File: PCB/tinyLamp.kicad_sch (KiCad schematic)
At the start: 21 parts, among them J11 USB_B_Mini, J12 Conn_02x03_Odd_Even, SW11 SW_Push, SW12 SW_Push, SW13 SW_Push, U11 TP4056, U12 ATtiny24A-SS, X11 BATT+, X12 BATT-

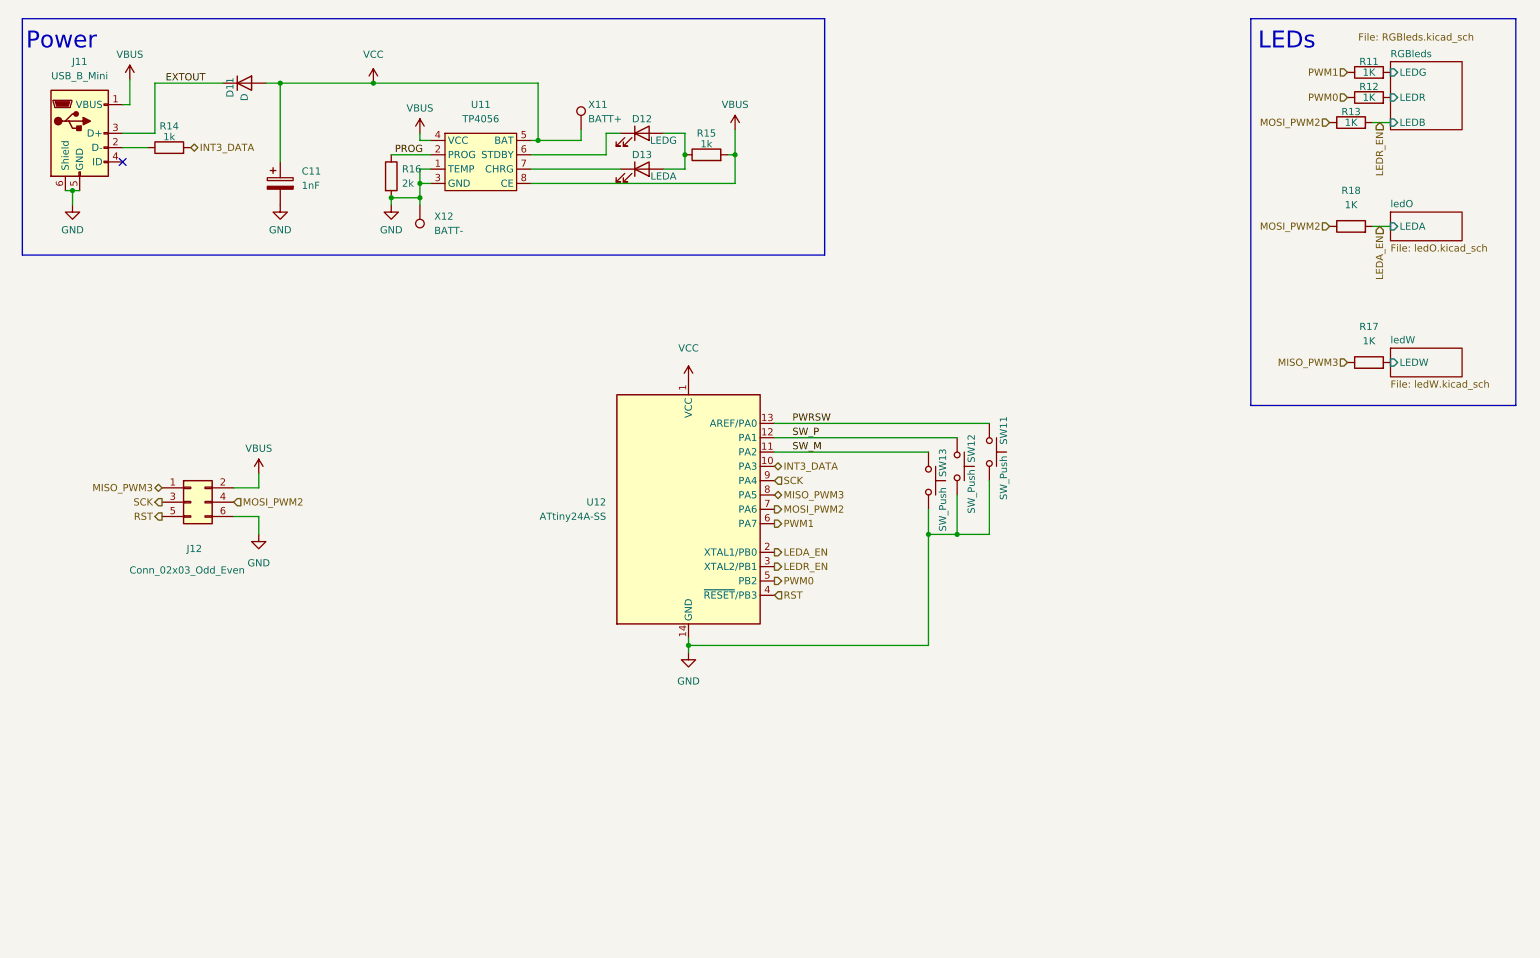
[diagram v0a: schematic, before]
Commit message: Updated Schematic to use Wemos D1 and external Power
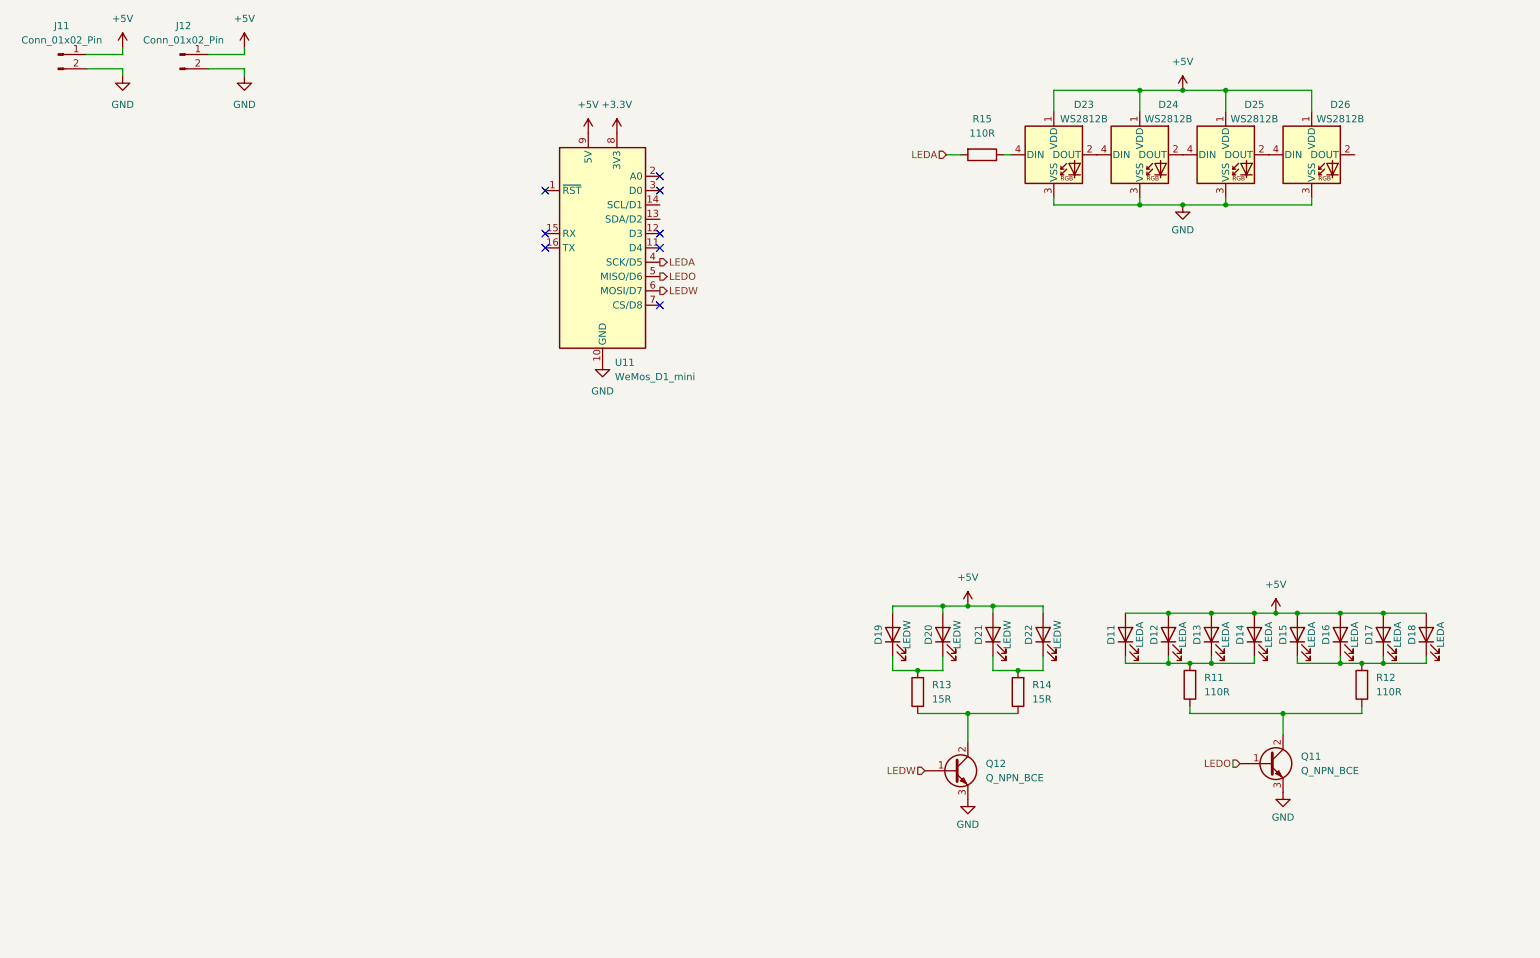
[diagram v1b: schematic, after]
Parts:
- removed C11: 1nF, Capacitor_SMD:C_1206_3216Metric_Pad1.33x1.80mm_HandSolder, symbol Device:C_Polarized
- removed D11: D, Diode_SMD:D_SOD-123, symbol Device:D
- removed J11: USB_B_Mini, Connector_USB:USB_Mini-B_Lumberg_2486_01_Horizontal, symbol Connector:USB_B_Mini
- removed J12: Conn_02x03_Odd_Even, Connector_PinHeader_2.54mm:PinHeader_2x03_P2.54mm_Vertical, symbol Connector_Generic:Conn_02x03_Odd_Even
- removed R16: 2k, Resistor_SMD:R_1206_3216Metric_Pad1.30x1.75mm_HandSolder, symbol Device:R
- removed R17, R18: 1K, Resistor_SMD:R_1206_3216Metric_Pad1.30x1.75mm_HandSolder, symbol Device:R
- removed SW11, SW12, SW13: SW_Push, Button_Switch_SMD:SW_SPST_CK_RS282G05A3, symbol Switch:SW_Push
- removed U11: TP4056, Package_SO:HSOP-8-1EP_3.9x4.9mm_P1.27mm_EP2.3x2.3mm, symbol BatteryProtection:TP4056
- removed U12: ATtiny24A-SS, Package_SO:SOIC-14_3.9x8.7mm_P1.27mm, symbol MCU_Microchip_ATtiny:ATtiny24A-SS
- removed X11: BATT+, TestPoint:TestPoint_Keystone_5015_Micro-Minature, symbol Connector:TestPoint
- removed X12: BATT-, TestPoint:TestPoint_Keystone_5015_Micro-Minature, symbol Connector:TestPoint
- added D11, D14, D15, D16, D17, D18: LEDA, LED_SMD:LED_0805_2012Metric_Pad1.15x1.40mm_HandSolder, symbol Device:LED
- added D19, D20, D21, D22: LEDW, LED_SMD:LED_PLCC-2, symbol Device:LED
- added D23, D24, D25, D26: WS2812B, LED_SMD:LED_WS2812B_PLCC4_5.0x5.0mm_P3.2mm, symbol LED:WS2812B
- added J11, J12: Conn_01x02_Pin, symbol Connector:Conn_01x02_Pin
- added Q11, Q12: Q_NPN_BCE, Package_TO_SOT_SMD:SOT-23, symbol Device:Q_NPN_BCE
- added U11: WeMos_D1_mini, Module:WEMOS_D1_mini_light, symbol MCU_Module:WeMos_D1_mini
- D12: value LEDG -> LEDA
- R11, R12: value 1K -> 110R; Price (none) -> 0.0021
- R13: value 1K -> 15R; Price (none) -> 0.0021
- R14: value 1k -> 15R
- R15: value 1k -> 110R
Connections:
- net MOSI_PWM2 is gone; now on an unnamed net: R13.1
- net PWM1 is gone; now on an unnamed net: R11.1
- net RGBleds/LEDG is gone; now on an unnamed net: R11.2
- net GND: now also D23.3 (VSS), D24.3 (VSS), D25.3 (VSS), D26.3 (VSS), J11.2 (Pin_2), J12.2 (Pin_2), Q11.3 (E), Q12.3 (E), U11.10 (GND)
- net at R14.1: now also Q12.2 (C)
- net at D12.1 (K): now also D13.1 (K), D11.1 (K), D14.1 (K)
- net +5V: now reaches D12.2 (A), D13.2 (A)
- net +5V: now also D11.2 (A), D14.2 (A), D15.2 (A), D16.2 (A), D17.2 (A), D18.2 (A), D19.2 (A), D20.2 (A), D21.2 (A), D22.2 (A), D23.1 (VDD), D24.1 (VDD), D25.1 (VDD), D26.1 (VDD), J11.1 (Pin_1), J12.1 (Pin_1), U11.9 (5V); no longer R15.1
- net INT3_DATA: no longer names the net of R14.2
- net INT3_DATA: now also D21.1 (K), D22.1 (K)
- net LEDR_EN: no longer names the net of R13.2
- net LEDR_EN: now also D19.1 (K), D20.1 (K)
- net PWM0: no longer names the net of R12.1
- net PWM0: now also Q11.2 (C)
- net RGBleds/LEDR: no longer names the net of R12.2
- net RGBleds/LEDR: now also D15.1 (K), D16.1 (K), D17.1 (K), D18.1 (K)
- net VBUS renamed LEDA
- net LEDA: now also U11.4 (SCK/D5)
- new net: D25.2 (DOUT), D26.4 (DIN)
- new net: D24.2 (DOUT), D25.4 (DIN)
- new net: D23.2 (DOUT), D24.4 (DIN)
- new net: D23.4 (DIN), R15.1
- new net +3.3V: U11.8 (3V3)
- new net LEDO: Q11.1 (B), U11.5 (MISO/D6)
- new net LEDW: Q12.1 (B), U11.6 (MOSI/D7)
- no-connect marks 1 -> 8
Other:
- removed sheet RGBleds
- removed sheet ledO
- removed sheet ledW
- note removed: "LEDs"
- note removed: "Power"

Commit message: made some changes
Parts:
- removed Q11, Q12: Q_NPN_BCE, Package_TO_SOT_SMD:SOT-23, symbol Device:Q_NPN_BCE
- added D23, D24, D25, D26: LED_O, LED_THT:LED_D3.0mm_FlatTop, symbol Device:LED
- added D31, D32: WS2812B, LED_SMD:LED_WS2812B_PLCC4_5.0x5.0mm_P3.2mm, symbol LED:WS2812B
- added Q11, Q12: BC547, Package_TO_SOT_THT:TO-92L_HandSolder, symbol Transistor_BJT:BC547
- D11, D12, D13, D14, D15, D16, D17, D18: value LEDA -> LED_W; footprint LED_SMD:LED_0805_2012Metric_Pad1.15x1.40mm_HandSolder -> LED_THT:LED_D3.0mm_FlatTop; Price 0.017 -> (none)
- D19, D20, D21, D22: value LEDW -> LED_O; footprint LED_SMD:LED_PLCC-2 -> LED_THT:LED_D3.0mm_FlatTop; Price 0.010 -> (none)
- J11, J12: footprint (none) -> Connector_PinHeader_2.54mm:PinHeader_1x02_P2.54mm_Vertical
- R11, R12, R15: footprint Resistor_SMD:R_1206_3216Metric_Pad1.30x1.75mm_HandSolder -> Resistor_THT:R_Axial_DIN0207_L6.3mm_D2.5mm_P10.16mm_Horizontal
- R13, R14: value 15R -> 110R; footprint Resistor_SMD:R_1206_3216Metric_Pad1.30x1.75mm_HandSolder -> Resistor_THT:R_Axial_DIN0207_L6.3mm_D2.5mm_P10.16mm_Horizontal
- renumbered D23 to D27, D24 to D28, D25 to D29, D26 to D30
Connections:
- net +5V: now also D23.2 (A), D25.2 (A), D31.1 (VDD), D32.1 (VDD); no longer D12.2 (A), D14.2 (A), D16.2 (A), D18.2 (A), D20.2 (A), D22.2 (A)
- net GND: now also D31.3 (VSS), D32.3 (VSS), Q11.3 (E), Q12.3 (E)
- net LEDO: now also R13.2
- net LEDW: now also R11.2
- net at D16.1 (K), D18.1 (K), R12.2: now also D12.1 (K), D14.1 (K); no longer D15.1 (K), D17.1 (K)
- net at R12.1: now also Q11.1 (C); no longer R11.1
- net at R14.1: now also Q12.1 (C); no longer R13.1
- net at D22.1 (K), R14.2: now also D20.1 (K), D24.1 (K), D26.1 (K); no longer D21.1 (K)
- net at D30.2 (DOUT): now also D31.4 (DIN)
- new net: D31.2 (DOUT), D32.4 (DIN)
- new net: D25.1 (K), D26.2 (A)
- new net: D23.1 (K), D24.2 (A)
- new net: D13.1 (K), D14.2 (A)
- new net: Q11.2 (B), R11.1
- new net: Q12.2 (B), R13.1
- new net: D11.1 (K), D12.2 (A)
- new net: D19.1 (K), D20.2 (A)
- new net: D15.1 (K), D16.2 (A)
- new net: D17.1 (K), D18.2 (A)
- new net: D21.1 (K), D22.2 (A)
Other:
- moved on the sheet: D27, D28, D29, D30, R15

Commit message: uploaded files
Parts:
- removed D19, D20, D21, D22, D23, D24, D25, D26: LED_O, LED_THT:LED_D3.0mm_FlatTop, symbol Device:LED
- removed Q12: BC547, Package_TO_SOT_THT:TO-92L_HandSolder, symbol Transistor_BJT:BC547
- removed R13, R14: 110R, Resistor_THT:R_Axial_DIN0207_L6.3mm_D2.5mm_P10.16mm_Horizontal, symbol Device:R
- added SW11, SW12: SW_Push, symbol Switch:SW_Push
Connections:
- net LEDO: no longer names the net of U11.5 (MISO/D6)

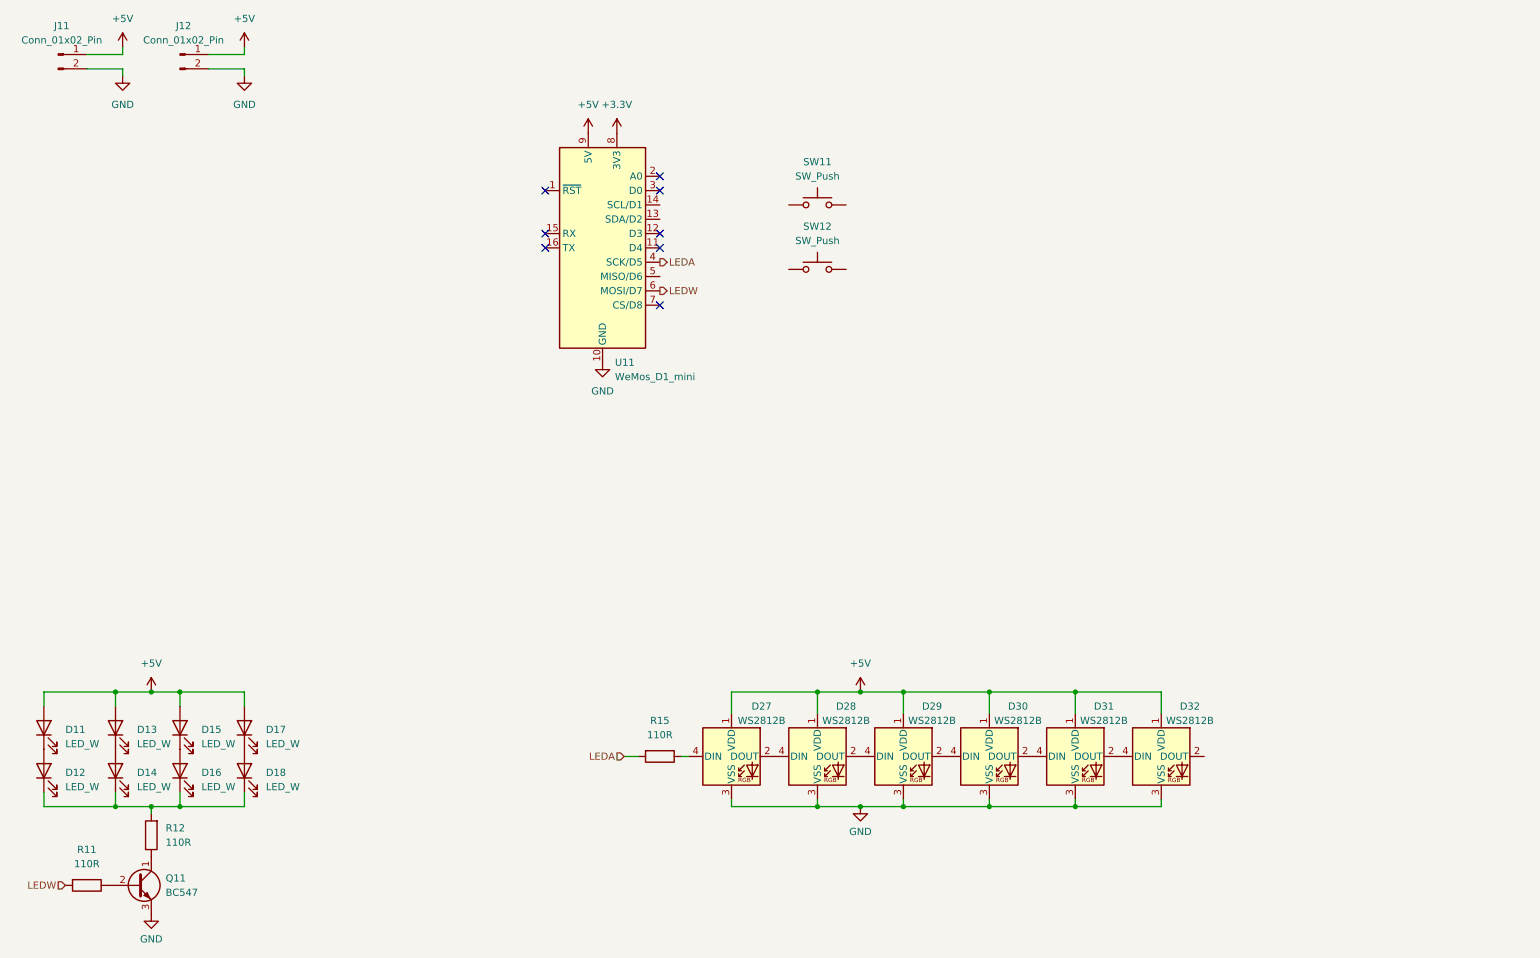
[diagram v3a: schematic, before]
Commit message: pcb: placed leds
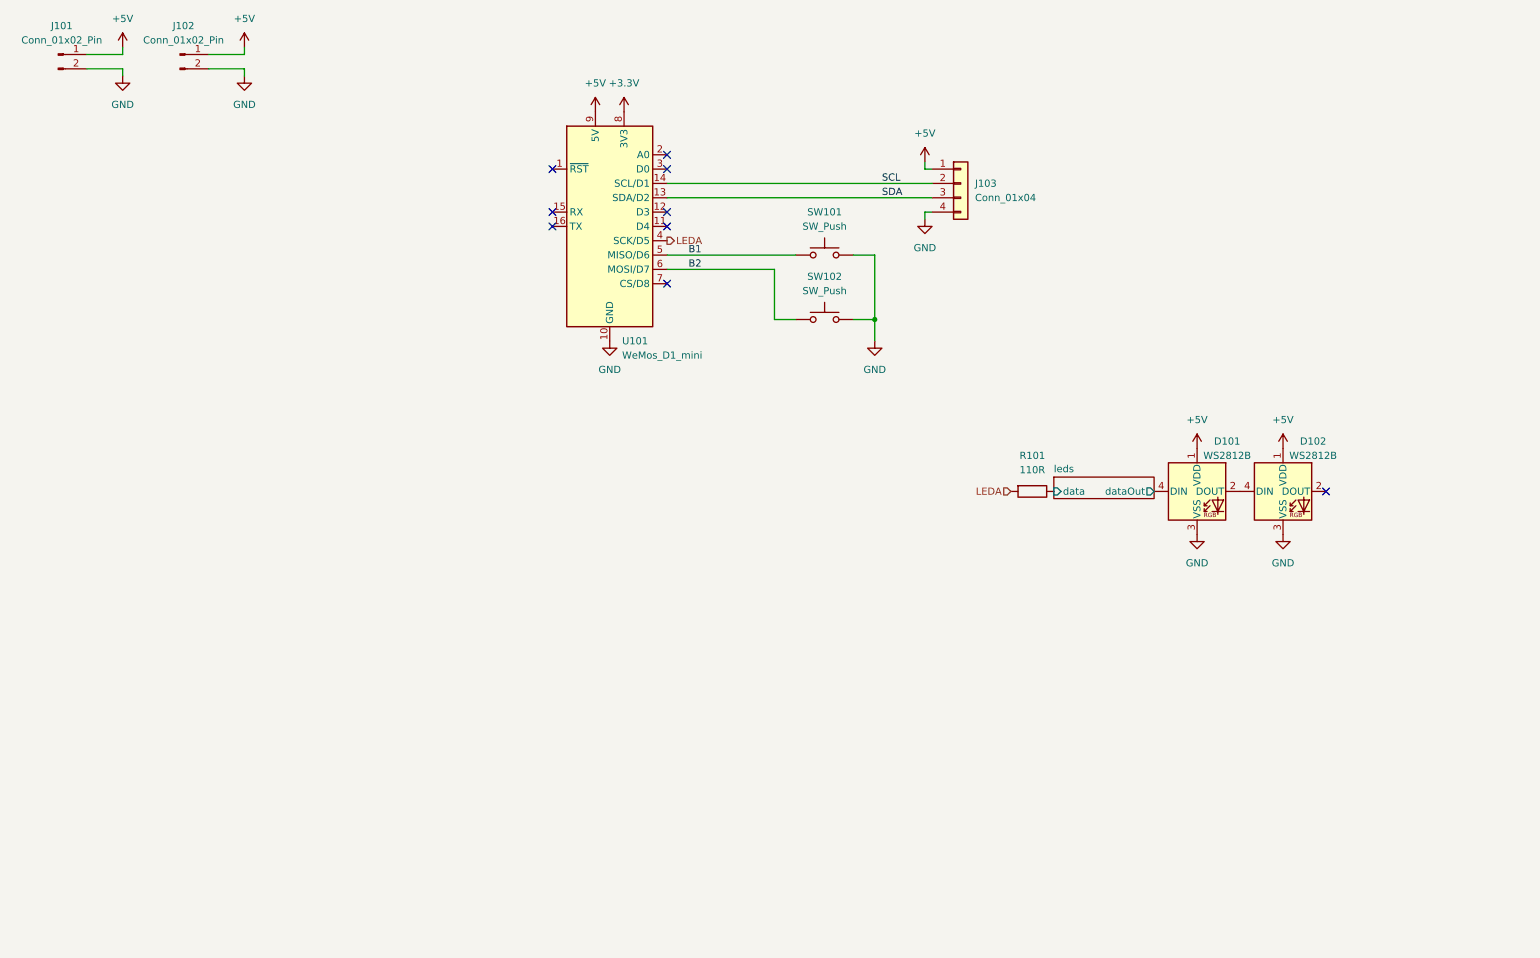
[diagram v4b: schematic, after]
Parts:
- removed D11, D12, D13, D14, D15, D16, D17, D18: LED_W, LED_THT:LED_D3.0mm_FlatTop, symbol Device:LED
- removed D27, D28, D29, D30, D31, D32: WS2812B, LED_SMD:LED_WS2812B_PLCC4_5.0x5.0mm_P3.2mm, symbol LED:WS2812B
- removed Q11: BC547, Package_TO_SOT_THT:TO-92L_HandSolder, symbol Transistor_BJT:BC547
- removed R11, R12, R15: 110R, Resistor_THT:R_Axial_DIN0207_L6.3mm_D2.5mm_P10.16mm_Horizontal, symbol Device:R
- added D101, D102: WS2812B, LED_SMD:LED_WS2812B_PLCC4_5.0x5.0mm_P3.2mm, symbol LED:WS2812B
- added J103: Conn_01x04, Connector_PinHeader_2.54mm:PinHeader_1x04_P2.54mm_Vertical, symbol Connector_Generic:Conn_01x04
- added R101: 110R, Resistor_THT:R_Axial_DIN0207_L6.3mm_D2.5mm_P10.16mm_Horizontal, symbol Device:R
- SW101: renamed from SW11; footprint (none) -> Button_Switch_SMD:SW_SPST_PTS647_Sx50
- SW102: renamed from SW12; footprint (none) -> Button_Switch_SMD:SW_SPST_PTS647_Sx50
- renumbered J11 to J101, J12 to J102, U11 to U101
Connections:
- net LEDW is gone; now on net B2: U101.6 (MOSI/D7)
- net +5V: now also D101.1 (VDD), D102.1 (VDD), J103.1 (Pin_1)
- net GND: now also SW101.2, SW102.2, D101.3 (VSS), D102.3 (VSS), J103.4 (Pin_4)
- net LEDA: now also R101.2
- net SDA: now reaches U101.13 (SDA/D2)
- net SDA: now also J103.3 (Pin_3)
- net SCL: now reaches U101.14 (SCL/D1)
- net SCL: now also J103.2 (Pin_2)
- net B1: now reaches U101.5 (MISO/D6)
- net B1: now also SW101.1
- net B2: now reaches SW102.1
- new net: D101.2 (DOUT), D102.4 (DIN)
- new net leds/data: R101.1
- new net leds/dataOut: D101.4 (DIN)
- no-connect marks 8 -> 9
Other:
- added sheet leds (leds.kicad_sch)
- moved on the sheet: SW101, SW102, U101
